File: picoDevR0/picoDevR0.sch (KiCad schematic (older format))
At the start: 10 parts, among them J1 Jack-DC, J2 Pico1to20, SW1 SW_MEC_5G, U1 LM1117-3.3

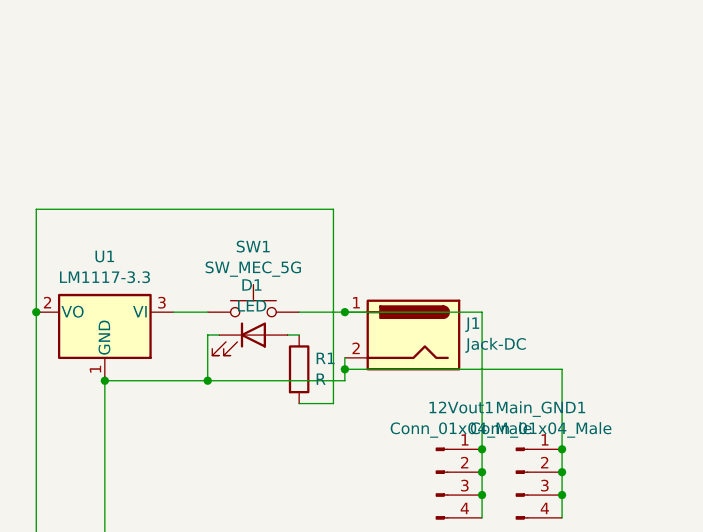
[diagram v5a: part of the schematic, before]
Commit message: fix switch and barrel jack
fixed only in sch, need changes in the PCBNew
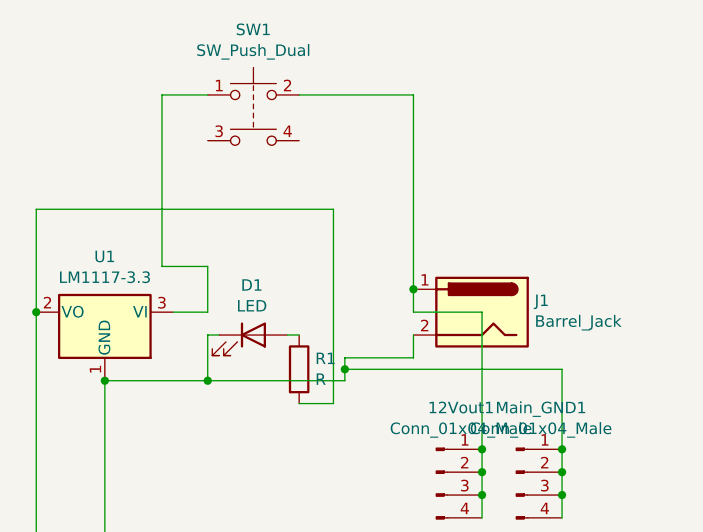
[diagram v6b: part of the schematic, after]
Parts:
- removed J1: Jack-DC, Connector_BarrelJack:BarrelJack_CUI_PJ-063AH_Horizontal, symbol Connector:Jack-DC
- removed SW1: SW_MEC_5G, Button_Switch_THT:SW_CW_GPTS203211B, symbol Switch:SW_MEC_5G
- added J1: Barrel_Jack, Connector_BarrelJack:BarrelJack_CUI_PJ-063AH_Horizontal, symbol Connector:Barrel_Jack
- added SW1: SW_Push_Dual, Button_Switch_THT:SW_PUSH-12mm, symbol Switch:SW_Push_Dual
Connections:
- net at D1.1 (K), Main_GND1.1 (Pin_1), Main_GND1.2 (Pin_2)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: now also J1.2
- net at U1.3 (VI): now also SW1.1
- net at 12Vout1.1 (Pin_1), 12Vout1.2 (Pin_2), 12Vout1.3 (Pin_3)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: now also J1.1, SW1.2
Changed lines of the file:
@@
 	5400 5650 6250 5650
-$Comp
-L Connector:Jack-DC J1
-U 1 1 60A0CA80
-P 6150 2300
-F 0 "J1" H 5920 2350 50  0000 R CNN
-F 1 "Jack-DC" H 5920 2259 50  0000 R CNN
-F 2 "Connector_BarrelJack:BarrelJack_CUI_PJ-063AH_Horizontal" H 6200 2260 50  0001 C CNN
-F 3 "~" H 6200 2260 50  0001 C CNN
-	1    6150 2300
-	-1   0    0    -1
-$EndComp
 $Comp
 L Regulator_Linear:LM1117-3.3 U1
@@
 Connection ~ 5400 3950
 Wire Wire Line
-	5650 2200 5850 2200
-Connection ~ 5850 2200
-Wire Wire Line
-	5850 2200 6450 2200
-Wire Wire Line
 	4800 2500 5250 2500
 Wire Wire Line
@@
 Connection ~ 4500 2200
 $Comp
-L Switch:SW_MEC_5G SW1
-U 1 1 60A09B24
-P 5450 2200
-F 0 "SW1" H 5450 2485 50  0000 C CNN
-F 1 "SW_MEC_5G" H 5450 2394 50  0000 C CNN
-F 2 "Button_Switch_THT:SW_CW_GPTS203211B" H 5450 2400 50  0001 C CNN
-F 3 "http://www.apem.com/int/index.php?controller=attachment&id_attachment=488" H 5450 2400 50  0001 C CNN
-	1    5450 2200
-	1    0    0    -1
-$EndComp
-$Comp
 L Device:LED D1
 U 1 1 60A0A221
@@
 Wire Wire Line
 	6450 3000 6450 2900
+$Comp
+L Connector:Barrel_Jack J1
+U 1 1 60A735D7
+P 6450 2200
+F 0 "J1" H 6220 2250 50  0000 R CNN
+F 1 "Barrel_Jack" H 6220 2159 50  0000 R CNN
+F 2 "Connector_BarrelJack:BarrelJack_CUI_PJ-063AH_Horizontal" H 6500 2160 50  0001 C CNN
+F 3 "~" H 6500 2160 50  0001 C CNN
+	1    6450 2200
+	-1   0    0    -1
+$EndComp
+Wire Wire Line
+	6450 2200 6150 2200
+Wire Wire Line
+	6150 2200 6150 2100
+Wire Wire Line
+	5850 2400 6150 2400
+Wire Wire Line
+	6150 2400 6150 2300
+Wire Wire Line
+	5650 1250 6150 1250
+Wire Wire Line
+	6150 1250 6150 2100
+Connection ~ 6150 2100
+$Comp
+L Switch:SW_Push_Dual SW1
+U 1 1 60A99454
+P 5450 1250
+F 0 "SW1" H 5450 1535 50  0000 C CNN
+F 1 "SW_Push_Dual" H 5450 1444 50  0000 C CNN
+F 2 "Button_Switch_THT:SW_PUSH-12mm" H 5450 1450 50  0001 C CNN
+F 3 "~" H 5450 1450 50  0001 C CNN
+	1    5450 1250
+	1    0    0    -1
+$EndComp
+Wire Wire Line
+	5250 1250 5050 1250
+Wire Wire Line
+	5050 1250 5050 2000
+Wire Wire Line
+	5050 2000 5250 2000
+Wire Wire Line
+	5250 2000 5250 2200
 $EndSCHEMATC

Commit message: changed LED and resistor footprint
earlier one's were too big
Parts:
- D1: footprint LED_THT:LED_D10.0mm -> LED_THT:LED_D4.0mm
- R1: footprint Resistor_THT:R_Axial_DIN0922_L20.0mm_D9.0mm_P30.48mm_Horizontal -> Resistor_THT:R_Axial_DIN0411_L9.9mm_D3.6mm_P25.40mm_Horizontal
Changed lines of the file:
@@
 F 0 "R1" H 5720 2496 50  0000 L CNN
 F 1 "R" H 5720 2405 50  0000 L CNN
-F 2 "Resistor_THT:R_Axial_DIN0922_L20.0mm_D9.0mm_P30.48mm_Horizontal" V 5580 2450 50  0001 C CNN
+F 2 "Resistor_THT:R_Axial_DIN0411_L9.9mm_D3.6mm_P25.40mm_Horizontal" V 5580 2450 50  0001 C CNN
 F 3 "~" H 5650 2450 50  0001 C CNN
 	1    5650 2450
@@
 F 0 "D1" H 5443 2517 50  0000 C CNN
 F 1 "LED" H 5443 2426 50  0000 C CNN
-F 2 "LED_THT:LED_D10.0mm" H 5450 2300 50  0001 C CNN
+F 2 "LED_THT:LED_D4.0mm" H 5450 2300 50  0001 C CNN
 F 3 "~" H 5450 2300 50  0001 C CNN
 	1    5450 2300

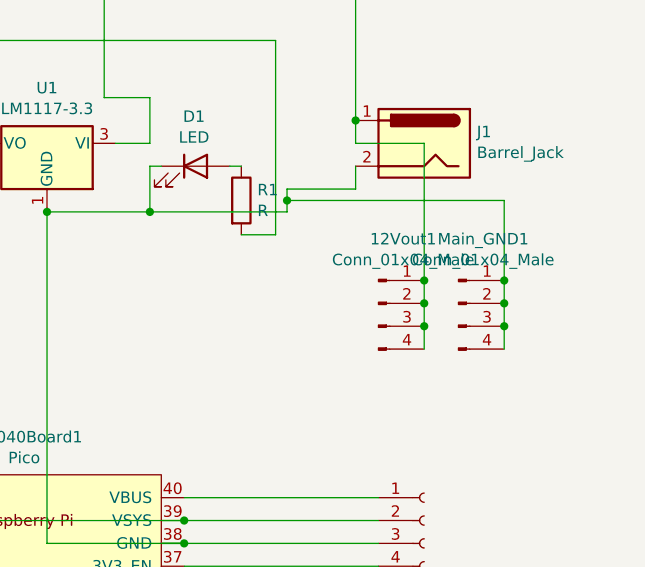
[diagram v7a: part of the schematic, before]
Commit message: added gnd layer
and removed all the gnd paths that were in place earlier
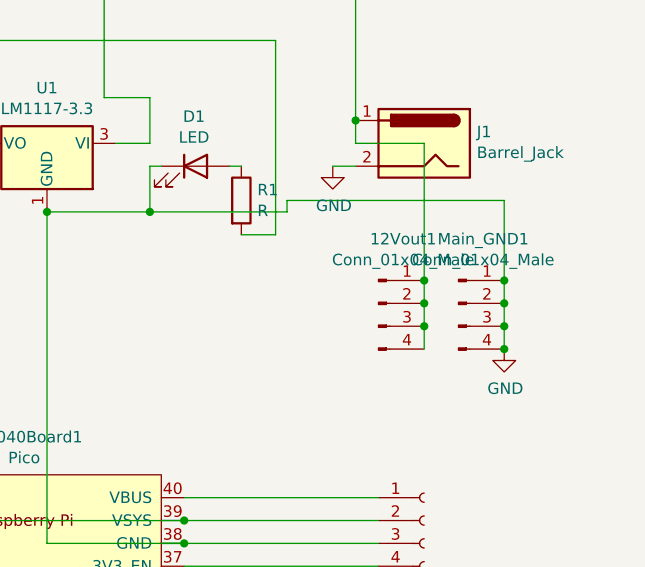
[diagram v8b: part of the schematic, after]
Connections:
- net GND: now reaches D1.1 (K), J1.2, Main_GND1.1 (Pin_1), Main_GND1.2 (Pin_2), Main_GND1.3 (Pin_3), Main_GND1.4 (Pin_4), RP2040Board1.38 (GND), U1.1 (GND), pico21to40.3 (Pin_3)
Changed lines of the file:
@@
 	-1   0    0    -1
 $EndComp
-Wire Wire Line
-	5850 2400 5850 2450
 $Comp
 L Connector:Conn_01x04_Male 12Vout1
@@
 Wire Wire Line
 	6800 2450 5850 2450
-Connection ~ 5850 2450
 Wire Wire Line
 	5850 2450 5850 2500
@@
 	6150 2200 6150 2100
 Wire Wire Line
-	5850 2400 6150 2400
-Wire Wire Line
-	6150 2400 6150 2300
-Wire Wire Line
 	5650 1250 6150 1250
 Wire Wire Line
@@
 Wire Wire Line
 	5250 2000 5250 2200
+$Comp
+L power:GND #PWR0101
+U 1 1 60A1A8C9
+P 6050 2300
+F 0 "#PWR0101" H 6050 2050 50  0001 C CNN
+F 1 "GND" H 6055 2127 50  0000 C CNN
+F 2 "" H 6050 2300 50  0001 C CNN
+F 3 "" H 6050 2300 50  0001 C CNN
+	1    6050 2300
+	1    0    0    -1
+$EndComp
+Wire Wire Line
+	6150 2300 6050 2300
+$Comp
+L power:GND #PWR0102
+U 1 1 60A24149
+P 6800 3100
+F 0 "#PWR0102" H 6800 2850 50  0001 C CNN
+F 1 "GND" H 6805 2927 50  0000 C CNN
+F 2 "" H 6800 3100 50  0001 C CNN
+F 3 "" H 6800 3100 50  0001 C CNN
+	1    6800 3100
+	1    0    0    -1
+$EndComp
+Connection ~ 6800 3100
 $EndSCHEMATC
